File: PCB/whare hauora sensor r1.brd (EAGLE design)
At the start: 21 parts, among them IC1 MEGA328P-AU, IC2 AT25DF512C-SSHN-B, IC3 SI7021, IC4 ATSHA204A

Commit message: 1st Rev PCB Design
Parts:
- added U$1: (no value), Callum:WHAREHAUORA
- IC2: value AT25DF512C-SSHN-B -> AT25DF512C; device microchip:SO-08 -> Callum:SO8
- moved C3 70.1 mm to (19.3, 48.5), turned to 0 degrees
- moved C6 58.6 mm to (27.9, 39.4), turned to 180 degrees
- moved D1 57.4 mm to (10.2, 53.3), flipped to the bottom, turned to 0 degrees
- moved JP3 57.2 mm to (21.6, 54.6)
- moved BATT1 55.9 mm to (4.83, 16.5)
- moved C2 55.9 mm to (19.3, 47.0)
- moved IC1 55.9 mm to (19.7, 40.6)
- moved JP2 55.9 mm to (6.35, 50.8)
- moved C5 55.9 mm to (11.4, 38.1)
- moved R3 55.9 mm to (11.4, 40.3)
- moved IC4 55.9 mm to (11.4, 42.8)
- moved C4 55.9 mm to (33.3, 49.1)
- moved IC2 55.9 mm to (35.7, 44.5), turned to 270 degrees
- moved R5 55.9 mm to (36.8, 50.8)
- moved R6 55.9 mm to (33.3, 50.8)
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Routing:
- net SCL: track 0.00 -> 71.9 mm, vias 0 -> 2
- net SDA: track 0.00 -> 70.5 mm, vias 0 -> 2
- net V+: track 114.8 -> 154.7 mm, vias 1 -> 3
- net GND: track 0.00 -> 11.4 mm
- net N$3: track 0.00 -> 9.14 mm, vias 0 -> 1
- net A2: track 0.00 -> 3.85 mm
- net RST: track 19.6 -> 21.8 mm
- net D2: track 23.1 -> 21.8 mm
- net D10: track 23.1 -> 21.8 mm
- net D9: track 13.4 -> 12.3 mm
- net D8: track 27.6 -> 26.6 mm
- net DTR: track 4.83 -> 4.32 mm
- net A3: track 3.05 -> 3.56 mm
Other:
- board outline added: 67.3 x 64.8 mm

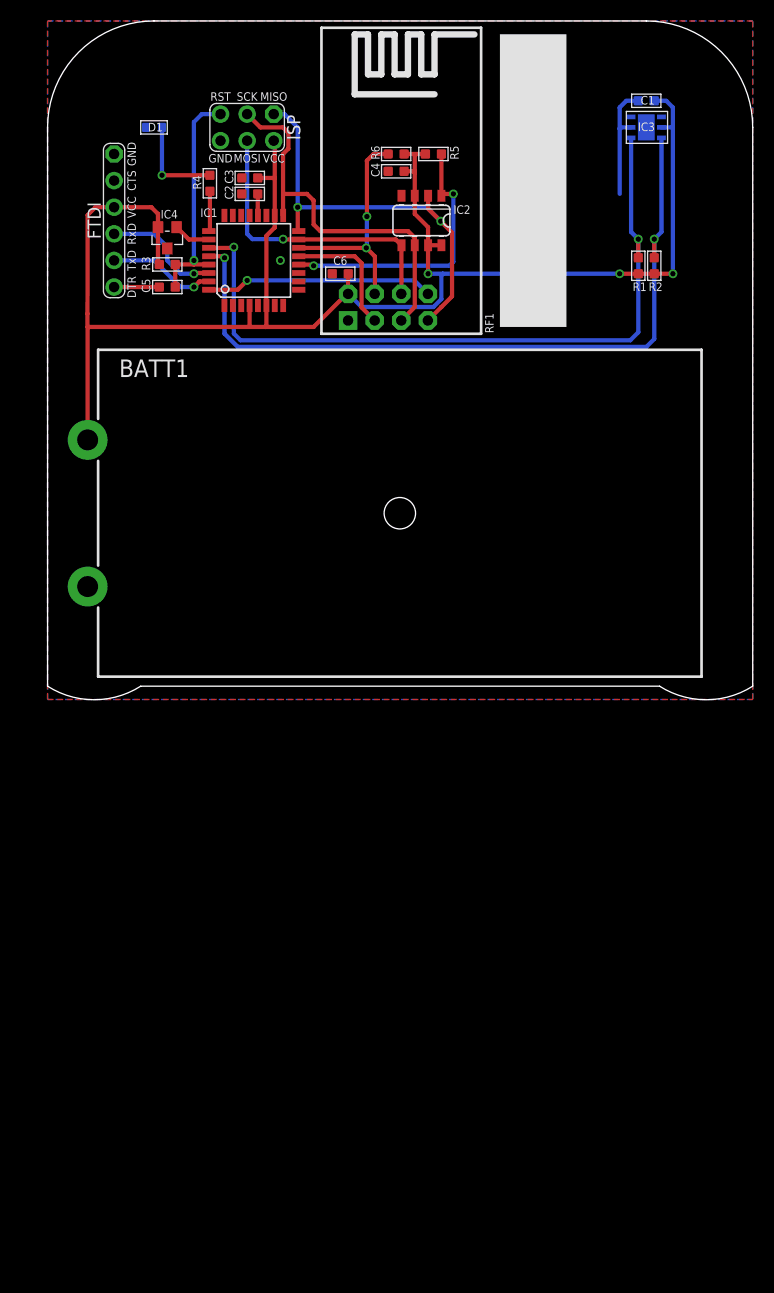
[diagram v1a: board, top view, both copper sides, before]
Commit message: PCB Update to 1.1
Reduced overall sivze of PCB
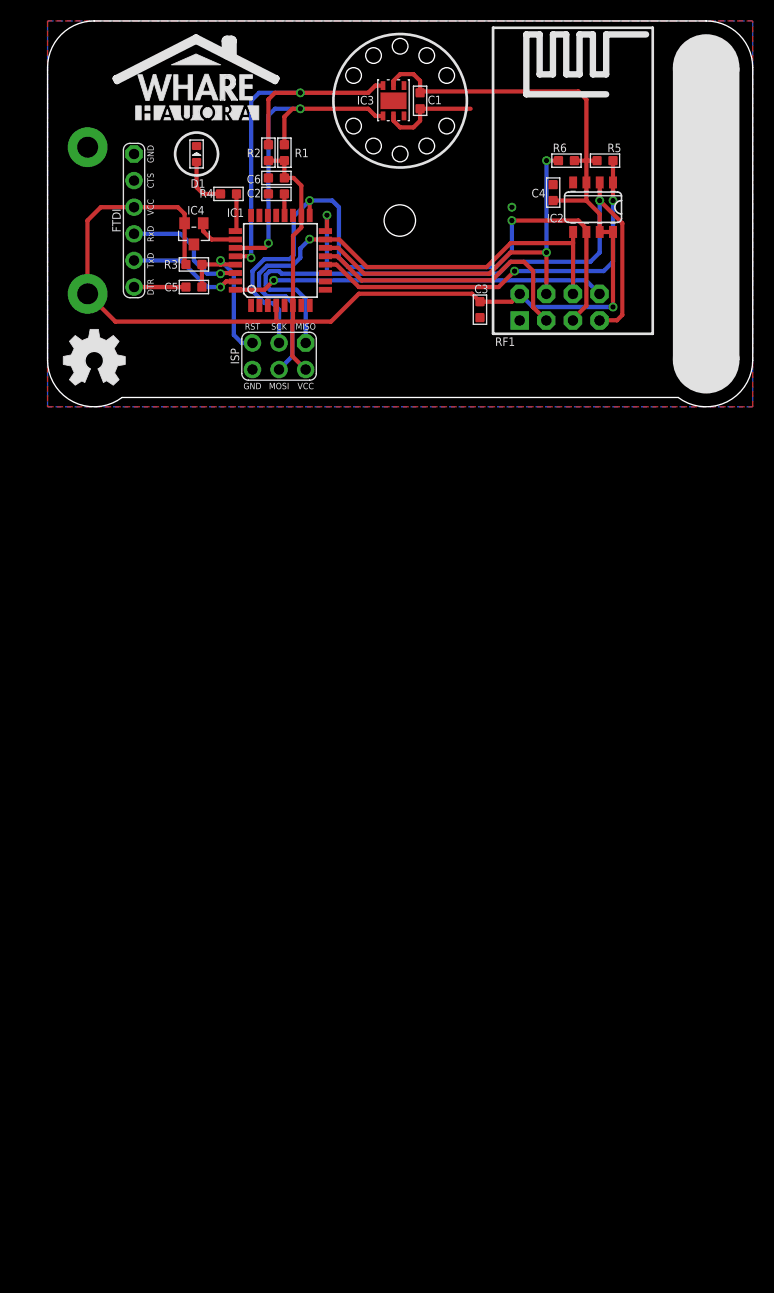
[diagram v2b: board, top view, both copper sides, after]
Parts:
- added U$2: (no value), Callum:WHAREHAUORA-SMALL
- added U$4: (no value), Callum:MY-LOGO-SMALL
- U$1: device Callum:WHAREHAUORA -> Callum:OSHW-LOGO
- moved U$1 58.7 mm to (4.45, 31.1), flipped to the top
- moved R2 38.4 mm to (21.1, 50.9)
- moved R1 35.5 mm to (22.6, 50.9)
- moved BATT1 27.9 mm to (4.83, 44.5), flipped to the bottom, turned to 180 degrees
- moved C3 25.3 mm to (41.3, 35.9), turned to 90 degrees
- moved IC3 24.3 mm to (33.0, 55.9), flipped to the top, turned to 90 degrees
- moved JP3 22.1 mm to (24.6, 32.8)
- moved C1 21.6 mm to (35.6, 55.9), flipped to the top, turned to 270 degrees
- moved IC2 16.4 mm to (52.1, 45.7)
- moved R5 16.4 mm to (53.2, 50.2)
- moved RF1 16.4 mm to (45.1, 34.9)
- moved R6 16.3 mm to (49.5, 50.2)
- moved C4 15.1 mm to (48.3, 47.1), turned to 90 degrees
- moved C6 11.0 mm to (21.8, 48.5)
- moved D1 4.79 mm to (14.2, 50.8), flipped to the top, turned to 90 degrees
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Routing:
- net SDA: track 70.5 -> 31.6 mm
- net SCL: track 71.9 -> 37.4 mm
- net MISO: track 40.8 -> 70.6 mm
- net SCK: track 36.9 -> 65.2 mm, vias 0 -> 2
- net MOSI: track 28.7 -> 51.9 mm
- net D10: track 21.8 -> 36.9 mm
- net D9: track 12.3 -> 27.1 mm
- net D2: track 21.8 -> 35.7 mm
- net D8: track 26.6 -> 39.0 mm
- net RST: track 21.8 -> 15.5 mm
- net V+: track 154.7 -> 148.4 mm, vias 3 -> 1
- net N$3: track 9.14 -> 4.96 mm, vias 1 -> 0
- net GND: track 11.4 -> 9.49 mm
- net TXD: track 10.3 -> 11.0 mm
- net RXD: track 11.4 -> 12.0 mm
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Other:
- board size 67.3 x 64.8 mm -> 67.3 x 36.8 mm
- board text added: "WHARE HAUORA SENSOR"
- board text added: "r1.1 AUGUST 2017"

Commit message: Minor Track Change
Fix spacing of tracks under CPU
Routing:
- net MOSI: track 51.9 -> 52.5 mm
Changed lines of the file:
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@@
 <wire x1="23.368" y1="36.576" x2="22.733" y2="37.211" width="0.4064" layer="16"/>
 <wire x1="22.733" y1="37.211" x2="20.955" y2="37.211" width="0.4064" layer="16"/>
-<wire x1="20.955" y1="37.211" x2="20.193" y2="37.973" width="0.4064" layer="16"/>
-<wire x1="20.193" y1="37.973" x2="20.193" y2="39.37" width="0.4064" layer="16"/>
-<wire x1="20.193" y1="39.37" x2="20.955" y2="40.132" width="0.4064" layer="16"/>
-<wire x1="20.955" y1="40.132" x2="23.368" y2="40.132" width="0.4064" layer="16"/>
-<wire x1="23.368" y1="40.132" x2="24.13" y2="40.894" width="0.4064" layer="16"/>
-<wire x1="24.13" y1="40.894" x2="24.13" y2="41.783" width="0.4064" layer="16"/>
-<wire x1="24.13" y1="41.783" x2="25.019" y2="42.672" width="0.4064" layer="16"/>
+<wire x1="20.955" y1="37.211" x2="20.066" y2="38.1" width="0.4064" layer="16"/>
+<wire x1="20.066" y1="38.1" x2="20.066" y2="39.37" width="0.4064" layer="16"/>
+<wire x1="20.066" y1="39.37" x2="20.955" y2="40.259" width="0.4064" layer="16"/>
+<wire x1="20.955" y1="40.259" x2="24.257" y2="40.259" width="0.4064" layer="16"/>
+<wire x1="24.257" y1="40.259" x2="25.019" y2="41.021" width="0.4064" layer="16"/>
+<wire x1="25.019" y1="41.021" x2="25.019" y2="42.672" width="0.4064" layer="16"/>
 </signal>
 <signal name="MISO">
@@
 <wire x1="22.352" y1="39.37" x2="22.098" y2="39.624" width="0.4064" layer="16"/>
 <wire x1="22.098" y1="39.624" x2="21.209" y2="39.624" width="0.4064" layer="16"/>
-<wire x1="21.209" y1="39.624" x2="20.828" y2="39.243" width="0.4064" layer="16"/>
+<wire x1="21.209" y1="39.624" x2="20.701" y2="39.116" width="0.4064" layer="16"/>
 <wire x1="24.638" y1="32.766" x2="24.638" y2="36.957" width="0.4064" layer="16"/>
 <wire x1="24.638" y1="36.957" x2="23.749" y2="37.846" width="0.4064" layer="16"/>
 <wire x1="23.749" y1="37.846" x2="21.209" y2="37.846" width="0.4064" layer="16"/>
-<wire x1="21.209" y1="37.846" x2="20.828" y2="38.227" width="0.4064" layer="16"/>
-<wire x1="20.828" y1="38.227" x2="20.828" y2="39.243" width="0.4064" layer="16"/>
+<wire x1="21.209" y1="37.846" x2="20.701" y2="38.354" width="0.4064" layer="16"/>
+<wire x1="20.701" y1="38.354" x2="20.701" y2="39.116" width="0.4064" layer="16"/>
 </signal>
 <signal name="SCK">
@@
 <wire x1="22.098" y1="35.941" x2="21.463" y2="36.576" width="0.4064" layer="16"/>
 <wire x1="21.463" y1="36.576" x2="20.701" y2="36.576" width="0.4064" layer="16"/>
-<wire x1="20.701" y1="36.576" x2="19.558" y2="37.719" width="0.4064" layer="16"/>
-<wire x1="19.558" y1="37.719" x2="19.558" y2="39.624" width="0.4064" layer="16"/>
-<wire x1="19.558" y1="39.624" x2="20.701" y2="40.767" width="0.4064" layer="16"/>
-<wire x1="20.701" y1="40.767" x2="23.114" y2="40.767" width="0.4064" layer="16"/>
-<wire x1="23.114" y1="40.767" x2="23.495" y2="41.148" width="0.4064" layer="16"/>
-<wire x1="23.495" y1="41.148" x2="23.495" y2="44.831" width="0.4064" layer="16"/>
-<wire x1="23.495" y1="44.831" x2="25.019" y2="46.355" width="0.4064" layer="16"/>
+<wire x1="20.701" y1="36.576" x2="19.431" y2="37.846" width="0.4064" layer="16"/>
+<wire x1="19.431" y1="37.846" x2="19.431" y2="39.624" width="0.4064" layer="16"/>
+<wire x1="19.431" y1="39.624" x2="20.701" y2="40.894" width="0.4064" layer="16"/>
+<wire x1="20.701" y1="40.894" x2="23.622" y2="40.894" width="0.4064" layer="16"/>
+<wire x1="23.622" y1="40.894" x2="24.13" y2="41.402" width="0.4064" layer="16"/>
+<wire x1="24.13" y1="41.402" x2="24.13" y2="45.466" width="0.4064" layer="16"/>
+<wire x1="24.13" y1="45.466" x2="25.019" y2="46.355" width="0.4064" layer="16"/>
 </signal>
 <signal name="SCL">

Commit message: Minor Cosmetic Tweaks
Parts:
- renumbered BATT1 to BATT
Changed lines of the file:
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@@
 <layer number="37" name="tTest" color="7" fill="1" visible="no" active="yes"/>
 <layer number="38" name="bTest" color="7" fill="1" visible="no" active="yes"/>
-<layer number="39" name="tKeepout" color="4" fill="11" visible="no" active="yes"/>
+<layer number="39" name="tKeepout" color="4" fill="11" visible="yes" active="yes"/>
 <layer number="40" name="bKeepout" color="1" fill="11" visible="no" active="yes"/>
 <layer number="41" name="tRestrict" color="4" fill="10" visible="yes" active="yes"/>
@@
 <attribute name="VALUE" x="39.98685" y="62.21318125" size="1.778" layer="27" font="vector" ratio="10" rot="R270"/>
 </element>
-<element name="BATT1" library="Callum" package="2AA-PACK\" value="2AA-PACK" x="4.826" y="44.45" rot="MR180"/>
+<element name="BATT" library="Callum" package="2AA-PACK\" value="2AA-PACK" x="4.826" y="44.45" smashed="yes" rot="MR180">
+<attribute name="NAME" x="53.816" y="31.45" size="1.6764" layer="26" ratio="10" rot="MR180"/>
+</element>
 <element name="IC2" library="Callum" package="SO8" value="AT25DF512C" x="52.07" y="45.72" smashed="yes" rot="R270">
 <attribute name="VALUE" x="50.292" y="44.577" size="0.4064" layer="27" ratio="10"/>
@@
 <vertex x="0" y="63.5"/>
 </polygon>
-<contactref element="BATT1" pad="-"/>
+<contactref element="BATT" pad="-"/>
 <via x="44.323" y="45.72" extent="1-16" drill="0.5"/>
 <polygon width="0.4064" layer="16">
@@
 <wire x1="24.225" y1="44.9326" x2="24.225" y2="43.783" width="0.4064" layer="1"/>
 <wire x1="24.225" y1="43.783" x2="23.425" y2="42.983" width="0.4064" layer="1"/>
-<contactref element="BATT1" pad="+"/>
+<contactref element="BATT" pad="+"/>
 <wire x1="13.081" y1="44.196" x2="13.081" y2="40.259" width="0.4064" layer="1"/>
 <wire x1="13.081" y1="40.259" x2="13.208" y2="40.259" width="0.4064" layer="1"/>
@@
 <wire x1="25.019" y1="44.9386" x2="25.025" y2="44.9326" width="0.4064" layer="1"/>
 <contactref element="IC2" pad="6"/>
-<wire x1="50.14685" y1="34.90818125" x2="50.14685" y2="35.03385" width="0.4064" layer="1"/>
-<wire x1="50.14685" y1="35.03385" x2="51.435" y2="36.322" width="0.4064" layer="1"/>
-<wire x1="51.435" y1="36.322" x2="51.435" y2="43.3578" width="0.4064" layer="1"/>
+<wire x1="50.14685" y1="34.90818125" x2="50.14685" y2="34.90685" width="0.4064" layer="1"/>
+<wire x1="50.14685" y1="34.90685" x2="51.435" y2="36.195" width="0.4064" layer="1"/>
+<wire x1="51.435" y1="36.195" x2="51.435" y2="43.3578" width="0.4064" layer="1"/>
 <wire x1="51.435" y1="43.3578" x2="51.435" y2="43.688" width="0.4064" layer="1"/>
 <wire x1="51.435" y1="43.688" x2="50.673" y2="44.45" width="0.4064" layer="1"/>

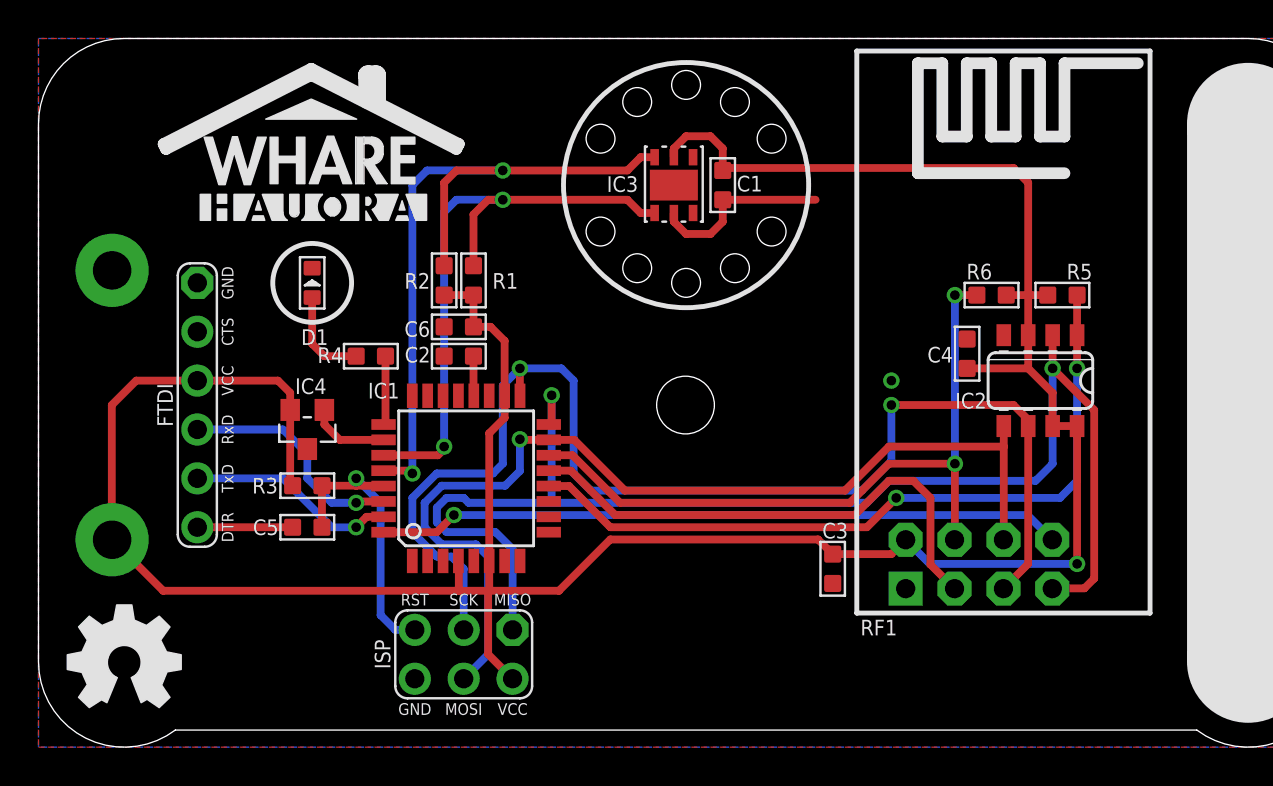
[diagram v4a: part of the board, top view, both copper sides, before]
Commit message: Minor Update
Moved batt holder for better balance & ISP header. Updated some overlays & footprints
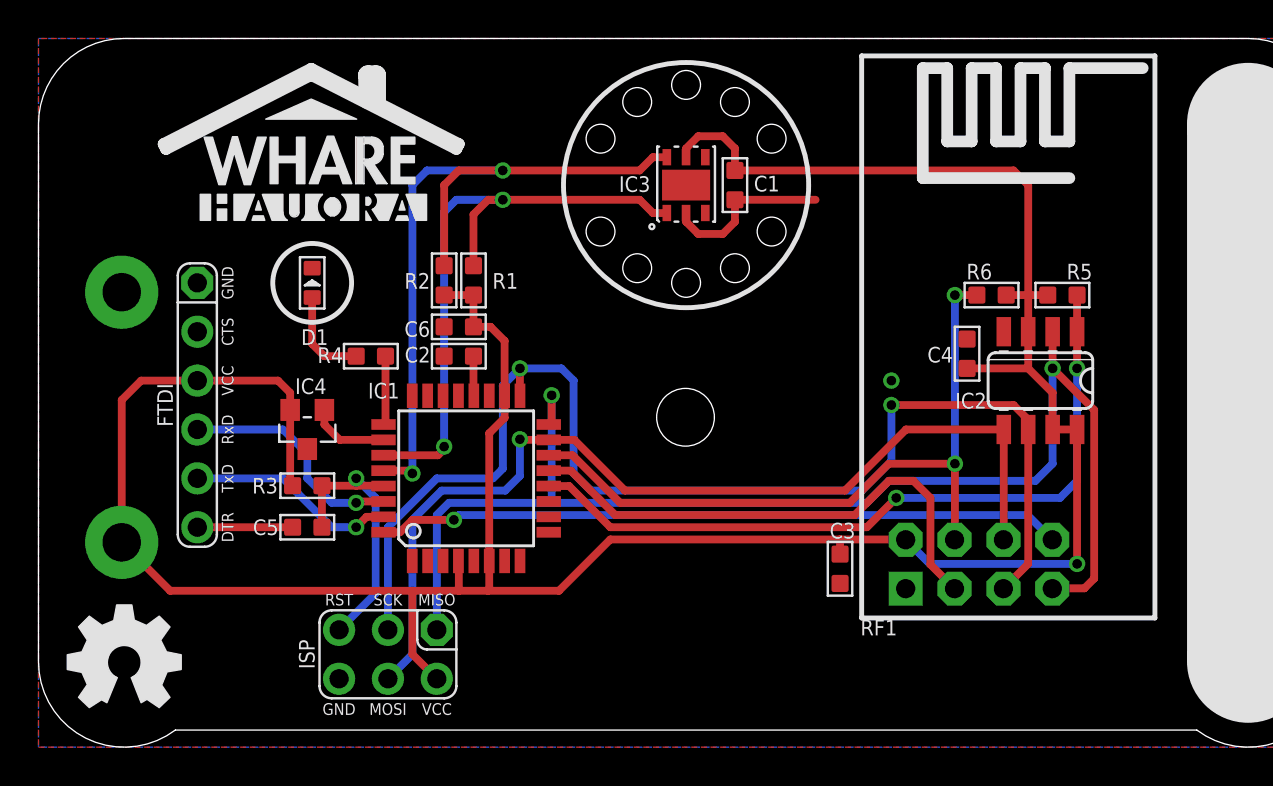
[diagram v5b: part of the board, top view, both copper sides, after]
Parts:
- moved JP3 3.94 mm to (20.7, 32.8)
- moved BATT 0.64 mm to (4.83, 43.8)
- moved C1 0.63 mm to (36.2, 55.9)
- moved IC3 0.63 mm to (33.7, 55.9)
- moved C3 0.38 mm to (41.7, 35.9)
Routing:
- net MISO: track 70.7 -> 67.3 mm
- net MOSI: track 52.5 -> 50.5 mm
- net V+: track 148.4 -> 147.0 mm
- net SCK: track 65.6 -> 64.6 mm
- net RST: track 15.5 -> 14.8 mm
- net GND: track 9.49 -> 8.86 mm
- net SDA: track 31.6 -> 32.2 mm
- net SCL: track 37.4 -> 37.9 mm
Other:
- board text added: "0.1u"
- board text added: "10k"
- board text added: "330"
- board text added: "4k7"
- board text added: "4u7"
- board text added: "56k"
- board text added: "ATSHA204A"
- board text added: "COMPONENT REFERENCE"
- board text added: "MEGA328P"
- board text added: "SI7021"
